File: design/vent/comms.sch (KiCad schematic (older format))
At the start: 23 parts, among them J11 SD_Card_modified, U1 R-78E3.3-0.5, U2 SN74LVC2T45, U3 XBEE_SC1, U4 SN74LVC2T45, U5 SN74LVC2T45

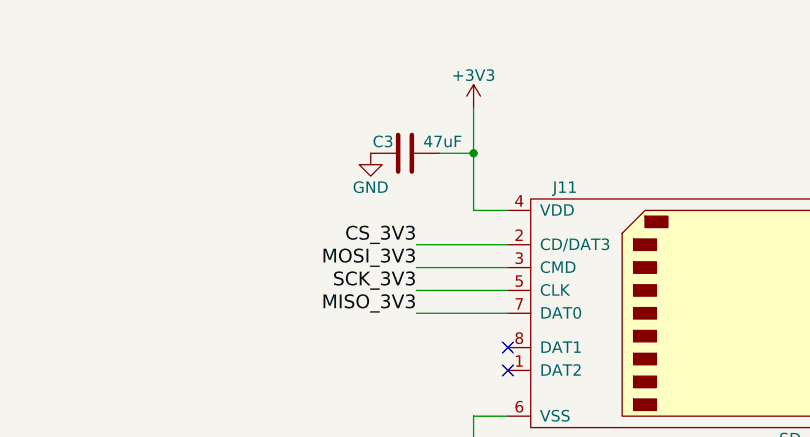
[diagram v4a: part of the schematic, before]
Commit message: Vent & Injector Board Layout
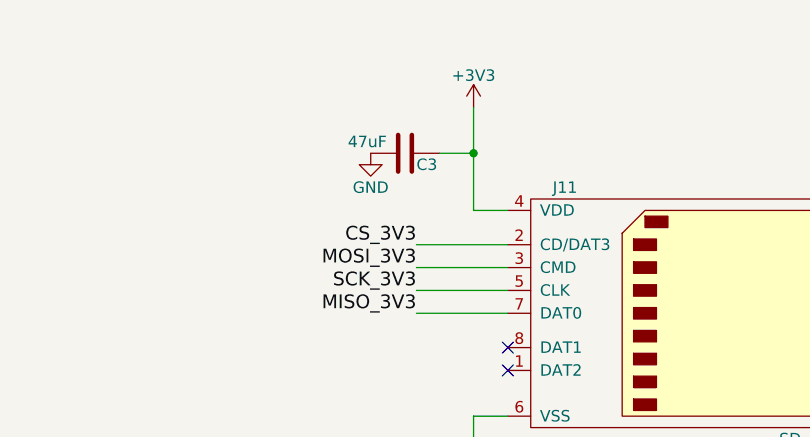
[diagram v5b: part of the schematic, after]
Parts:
- C3: footprint Capacitors_SMD:C_0805_HandSoldering -> Capacitors_ThroughHole:CP_Radial_Tantal_D5.0mm_P2.50mm
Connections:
- net +3V3: now also C3.1; no longer C3.2
- net GND: now also C3.2; no longer C3.1
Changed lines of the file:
@@
 $EndComp
 $Comp
-L GND #PWR011
+L GND #PWR09
 U 1 1 5AE12437
 P 7600 3050
-F 0 "#PWR011" H 7600 2800 50  0001 C CNN
+F 0 "#PWR09" H 7600 2800 50  0001 C CNN
 F 1 "GND" H 7600 2900 50  0000 C CNN
 F 2 "" H 7600 3050 50  0001 C CNN
@@
 NoConn ~ 7750 2750
 $Comp
-L +3V3 #PWR012
+L +3V3 #PWR010
 U 1 1 5AE1243F
 P 7600 1600
-F 0 "#PWR012" H 7600 1450 50  0001 C CNN
+F 0 "#PWR010" H 7600 1450 50  0001 C CNN
 F 1 "+3V3" H 7600 1740 50  0000 C CNN
 F 2 "" H 7600 1600 50  0001 C CNN
@@
 $EndComp
 $Comp
-L GND #PWR013
+L GND #PWR011
 U 1 1 5AE89456
 P 7750 5700
-F 0 "#PWR013" H 7750 5450 50  0001 C CNN
+F 0 "#PWR011" H 7750 5450 50  0001 C CNN
 F 1 "GND" H 7750 5550 50  0000 C CNN
 F 2 "" H 7750 5700 50  0001 C CNN
@@
 $EndComp
 $Comp
-L GND #PWR014
+L GND #PWR012
 U 1 1 5AE89479
 P 8300 4250
-F 0 "#PWR014" H 8300 4000 50  0001 C CNN
+F 0 "#PWR012" H 8300 4000 50  0001 C CNN
 F 1 "GND" H 8300 4100 50  0000 C CNN
 F 2 "" H 8300 4250 50  0001 C CNN
@@
 $EndComp
 $Comp
-L GND #PWR015
+L GND #PWR013
 U 1 1 5AE8947F
 P 7900 4250
-F 0 "#PWR015" H 7900 4000 50  0001 C CNN
+F 0 "#PWR013" H 7900 4000 50  0001 C CNN
 F 1 "GND" H 7900 4100 50  0000 C CNN
 F 2 "" H 7900 4250 50  0001 C CNN
@@
 $EndComp
 $Comp
-L +3V3 #PWR016
+L +3V3 #PWR014
 U 1 1 5AE89485
 P 7650 3750
-F 0 "#PWR016" H 7650 3600 50  0001 C CNN
+F 0 "#PWR014" H 7650 3600 50  0001 C CNN
 F 1 "+3V3" H 7650 3890 50  0000 C CNN
 F 2 "" H 7650 3750 50  0001 C CNN
@@
 $EndComp
 $Comp
-L GND #PWR017
+L GND #PWR015
 U 1 1 5AE89E54
 P 2600 2000
-F 0 "#PWR017" H 2600 1750 50  0001 C CNN
+F 0 "#PWR015" H 2600 1750 50  0001 C CNN
 F 1 "GND" H 2600 1850 50  0000 C CNN
 F 2 "" H 2600 2000 50  0001 C CNN
@@
 $EndComp
 $Comp
-L GND #PWR018
+L GND #PWR016
 U 1 1 5AE89E5A
 P 3350 2000
-F 0 "#PWR018" H 3350 1750 50  0001 C CNN
+F 0 "#PWR016" H 3350 1750 50  0001 C CNN
 F 1 "GND" H 3350 1850 50  0000 C CNN
 F 2 "" H 3350 2000 50  0001 C CNN
@@
 $EndComp
 $Comp
-L GND #PWR019
+L GND #PWR017
 U 1 1 5AE89E61
 P 4250 2000
-F 0 "#PWR019" H 4250 1750 50  0001 C CNN
+F 0 "#PWR017" H 4250 1750 50  0001 C CNN
 F 1 "GND" H 4250 1850 50  0000 C CNN
 F 2 "" H 4250 2000 50  0001 C CNN
@@
 $EndComp
 $Comp
-L +11.1V #PWR020
+L +11.1V #PWR018
 U 1 1 5AE89E6C
 P 2600 1400
-F 0 "#PWR020" H 2600 1250 50  0001 C CNN
+F 0 "#PWR018" H 2600 1250 50  0001 C CNN
 F 1 "+11.1V" H 2600 1540 50  0000 C CNN
 F 2 "" H 2600 1400 50  0001 C CNN
@@
 $EndComp
 $Comp
-L +3V3 #PWR021
+L +3V3 #PWR019
 U 1 1 5AE89E73
 P 4250 1400
-F 0 "#PWR021" H 4250 1250 50  0001 C CNN
+F 0 "#PWR019" H 4250 1250 50  0001 C CNN
 F 1 "+3V3" H 4250 1540 50  0000 C CNN
 F 2 "" H 4250 1400 50  0001 C CNN
@@
 $EndComp
 $Comp
-L GND #PWR022
+L GND #PWR020
 U 1 1 5AE8BD09
 P 2900 7050
-F 0 "#PWR022" H 2900 6800 50  0001 C CNN
+F 0 "#PWR020" H 2900 6800 50  0001 C CNN
 F 1 "GND" H 2900 6900 50  0000 C CNN
 F 2 "" H 2900 7050 50  0001 C CNN
@@
 $EndComp
 $Comp
-L GND #PWR023
+L GND #PWR021
 U 1 1 5AE8BD14
 P 4150 7050
-F 0 "#PWR023" H 4150 6800 50  0001 C CNN
+F 0 "#PWR021" H 4150 6800 50  0001 C CNN
 F 1 "GND" H 4150 6900 50  0000 C CNN
 F 2 "" H 4150 7050 50  0001 C CNN
@@
 XBEE_DOUT_3V3
 $Comp
-L +5V #PWR024
+L +5V #PWR022
 U 1 1 5AEA6163
 P 2900 6150
-F 0 "#PWR024" H 2900 6000 50  0001 C CNN
+F 0 "#PWR022" H 2900 6000 50  0001 C CNN
 F 1 "+5V" H 2900 6290 50  0000 C CNN
 F 2 "" H 2900 6150 50  0001 C CNN
@@
 $EndComp
 $Comp
-L +3V3 #PWR025
+L +3V3 #PWR023
 U 1 1 5AEA616A
 P 4150 6150
-F 0 "#PWR025" H 4150 6000 50  0001 C CNN
+F 0 "#PWR023" H 4150 6000 50  0001 C CNN
 F 1 "+3V3" H 4150 6290 50  0000 C CNN
 F 2 "" H 4150 6150 50  0001 C CNN
@@
 $EndComp
 $Comp
-L GND #PWR026
+L GND #PWR024
 U 1 1 5AEA6178
 P 4700 6350
-F 0 "#PWR026" H 4700 6100 50  0001 C CNN
+F 0 "#PWR024" H 4700 6100 50  0001 C CNN
 F 1 "GND" H 4700 6200 50  0000 C CNN
 F 2 "" H 4700 6350 50  0001 C CNN
@@
 $EndComp
 $Comp
-L GND #PWR027
+L GND #PWR025
 U 1 1 5AEA6189
 P 2350 6350
-F 0 "#PWR027" H 2350 6100 50  0001 C CNN
+F 0 "#PWR025" H 2350 6100 50  0001 C CNN
 F 1 "GND" H 2350 6200 50  0000 C CNN
 F 2 "" H 2350 6350 50  0001 C CNN
@@
 P 7300 1800
 F 0 "C3" V 7350 1850 50  0000 L CNN
-F 1 "47uF" V 7350 1550 50  0000 L CNN
-F 2 "Capacitors_SMD:C_0805_HandSoldering" H 7338 1650 50  0001 C CNN
+F 1 "47uF" V 7250 1550 50  0000 L CNN
+F 2 "Capacitors_ThroughHole:CP_Radial_Tantal_D5.0mm_P2.50mm" H 7338 1650 50  0001 C CNN
 F 3 "" H 7300 1800 50  0001 C CNN
 	1    7300 1800
-	0    -1   -1   0
-$EndComp
-$Comp
-L GND #PWR028
+	0    1    1    0
+$EndComp
+$Comp
+L GND #PWR026
 U 1 1 5AEA6BEA
 P 7150 1800
-F 0 "#PWR028" H 7150 1550 50  0001 C CNN
+F 0 "#PWR026" H 7150 1550 50  0001 C CNN
 F 1 "GND" H 7150 1650 50  0000 C CNN
 F 2 "" H 7150 1800 50  0001 C CNN
@@
 $EndComp
 $Comp
-L GND #PWR029
+L GND #PWR027
 U 1 1 5AE8B911
 P 2950 5550
-F 0 "#PWR029" H 2950 5300 50  0001 C CNN
+F 0 "#PWR027" H 2950 5300 50  0001 C CNN
 F 1 "GND" H 2950 5400 50  0000 C CNN
 F 2 "" H 2950 5550 50  0001 C CNN
@@
 $EndComp
 $Comp
-L GND #PWR030
+L GND #PWR028
 U 1 1 5AE8B906
 P 4200 5550
-F 0 "#PWR030" H 4200 5300 50  0001 C CNN
+F 0 "#PWR028" H 4200 5300 50  0001 C CNN
 F 1 "GND" H 4200 5400 50  0000 C CNN
 F 2 "" H 4200 5550 50  0001 C CNN
@@
 $EndComp
 $Comp
-L GND #PWR031
+L GND #PWR029
 U 1 1 5AEA5E4C
 P 2400 4850
-F 0 "#PWR031" H 2400 4600 50  0001 C CNN
+F 0 "#PWR029" H 2400 4600 50  0001 C CNN
 F 1 "GND" H 2400 4700 50  0000 C CNN
 F 2 "" H 2400 4850 50  0001 C CNN
@@
 $EndComp
 $Comp
-L GND #PWR032
+L GND #PWR030
 U 1 1 5AEA5E3B
 P 4750 4850
-F 0 "#PWR032" H 4750 4600 50  0001 C CNN
+F 0 "#PWR030" H 4750 4600 50  0001 C CNN
 F 1 "GND" H 4750 4700 50  0000 C CNN
 F 2 "" H 4750 4850 50  0001 C CNN
@@
 $EndComp
 $Comp
-L +3V3 #PWR033
+L +3V3 #PWR031
 U 1 1 5AEA5E2D
 P 4200 4650
-F 0 "#PWR033" H 4200 4500 50  0001 C CNN
+F 0 "#PWR031" H 4200 4500 50  0001 C CNN
 F 1 "+3V3" H 4200 4790 50  0000 C CNN
 F 2 "" H 4200 4650 50  0001 C CNN
@@
 $EndComp
 $Comp
-L +5V #PWR034
+L +5V #PWR032
 U 1 1 5AEA5E26
 P 2950 4650
-F 0 "#PWR034" H 2950 4500 50  0001 C CNN
+F 0 "#PWR032" H 2950 4500 50  0001 C CNN
 F 1 "+5V" H 2950 4790 50  0000 C CNN
 F 2 "" H 2950 4650 50  0001 C CNN
@@
 	2550 3250 2400 3250
 $Comp
-L GND #PWR035
+L GND #PWR033
 U 1 1 5AEA57E3
 P 2400 3350
-F 0 "#PWR035" H 2400 3100 50  0001 C CNN
+F 0 "#PWR033" H 2400 3100 50  0001 C CNN
 F 1 "GND" H 2400 3200 50  0000 C CNN
 F 2 "" H 2400 3350 50  0001 C CNN
@@
 	4600 3250 4750 3250
 $Comp
-L GND #PWR036
+L GND #PWR034
 U 1 1 5AEA4F48
 P 4750 3350
-F 0 "#PWR036" H 4750 3100 50  0001 C CNN
+F 0 "#PWR034" H 4750 3100 50  0001 C CNN
 F 1 "GND" H 4750 3200 50  0000 C CNN
 F 2 "" H 4750 3350 50  0001 C CNN
@@
 	2950 4050 2950 3950
 $Comp
-L GND #PWR037
+L GND #PWR035
 U 1 1 5AE8AFC0
 P 2950 4050
-F 0 "#PWR037" H 2950 3800 50  0001 C CNN
+F 0 "#PWR035" H 2950 3800 50  0001 C CNN
 F 1 "GND" H 2950 3900 50  0000 C CNN
 F 2 "" H 2950 4050 50  0001 C CNN
@@
 	4200 4050 4200 3950
 $Comp
-L GND #PWR038
+L GND #PWR036
 U 1 1 5AE8AA21
 P 4200 4050
-F 0 "#PWR038" H 4200 3800 50  0001 C CNN
+F 0 "#PWR036" H 4200 3800 50  0001 C CNN
 F 1 "GND" H 4200 3900 50  0000 C CNN
 F 2 "" H 4200 4050 50  0001 C CNN
@@
 	4200 3150 4200 3650
 $Comp
-L +3V3 #PWR039
+L +3V3 #PWR037
 U 1 1 5AE8A9C2
 P 4200 3150
-F 0 "#PWR039" H 4200 3000 50  0001 C CNN
+F 0 "#PWR037" H 4200 3000 50  0001 C CNN
 F 1 "+3V3" H 4200 3290 50  0000 C CNN
 F 2 "" H 4200 3150 50  0001 C CNN
@@
 	2950 3150 2950 3650
 $Comp
-L +5V #PWR040
+L +5V #PWR038
 U 1 1 5AE8A95E
 P 2950 3150
-F 0 "#PWR040" H 2950 3000 50  0001 C CNN
+F 0 "#PWR038" H 2950 3000 50  0001 C CNN
 F 1 "+5V" H 2950 3290 50  0000 C CNN
 F 2 "" H 2950 3150 50  0001 C CNN
@@
 $EndComp
 $Comp
-L +5V #PWR041
+L +5V #PWR039
 U 1 1 5AEF7DAE
 P 2100 3300
-F 0 "#PWR041" H 2100 3150 50  0001 C CNN
+F 0 "#PWR039" H 2100 3150 50  0001 C CNN
 F 1 "+5V" H 2100 3440 50  0000 C CNN
 F 2 "" H 2100 3300 50  0001 C CNN
@@
 $EndComp
 $Comp
-L +5V #PWR042
+L +5V #PWR040
 U 1 1 5AEF8338
 P 1900 3300
-F 0 "#PWR042" H 1900 3150 50  0001 C CNN
+F 0 "#PWR040" H 1900 3150 50  0001 C CNN
 F 1 "+5V" H 1900 3440 50  0000 C CNN
 F 2 "" H 1900 3300 50  0001 C CNN
@@
 $EndComp
 $Comp
-L +5V #PWR043
+L +5V #PWR041
 U 1 1 5AEF8BC1
 P 2100 4800
-F 0 "#PWR043" H 2100 4650 50  0001 C CNN
+F 0 "#PWR041" H 2100 4650 50  0001 C CNN
 F 1 "+5V" H 2100 4940 50  0000 C CNN
 F 2 "" H 2100 4800 50  0001 C CNN
@@
 $EndComp
 $Comp
-L +5V #PWR044
+L +5V #PWR042
 U 1 1 5AEF8BCE
 P 1900 4800
-F 0 "#PWR044" H 1900 4650 50  0001 C CNN
+F 0 "#PWR042" H 1900 4650 50  0001 C CNN
 F 1 "+5V" H 1900 4940 50  0000 C CNN
 F 2 "" H 1900 4800 50  0001 C CNN
@@
 Connection ~ 5250 6850
 $Comp
-L +3V3 #PWR045
+L +3V3 #PWR043
 U 1 1 5AF01235
 P 5050 6300
-F 0 "#PWR045" H 5050 6150 50  0001 C CNN
+F 0 "#PWR043" H 5050 6150 50  0001 C CNN
 F 1 "+3V3" H 5050 6440 50  0000 C CNN
 F 2 "" H 5050 6300 50  0001 C CNN
@@
 $EndComp
 $Comp
-L +3V3 #PWR046
+L +3V3 #PWR044
 U 1 1 5AF01329
 P 5250 6300
-F 0 "#PWR046" H 5250 6150 50  0001 C CNN
+F 0 "#PWR044" H 5250 6150 50  0001 C CNN
 F 1 "+3V3" H 5250 6440 50  0000 C CNN
 F 2 "" H 5250 6300 50  0001 C CNN

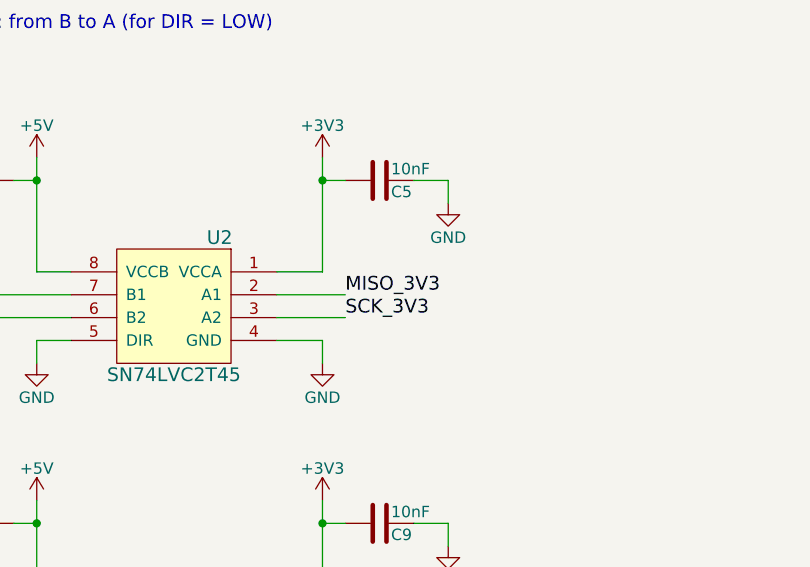
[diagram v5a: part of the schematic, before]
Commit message: Final vent/injector layout + routing
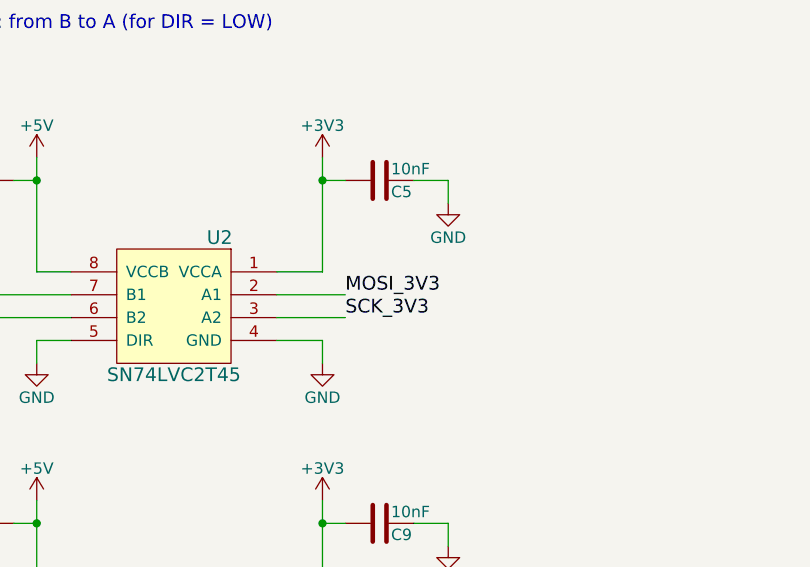
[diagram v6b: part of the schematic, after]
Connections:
- net MISO_3V3: no longer U2.2 (A1)
- net MOSI_3V3: now also U2.2 (A1)
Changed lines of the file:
@@
 $EndComp
 Text Label 4300 3750 0    60   ~ 0
-MISO_3V3
+MOSI_3V3
 Text Label 4300 3850 0    60   ~ 0
 SCK_3V3
